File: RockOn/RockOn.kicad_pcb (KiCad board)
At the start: 2 copper layers, 10 parts

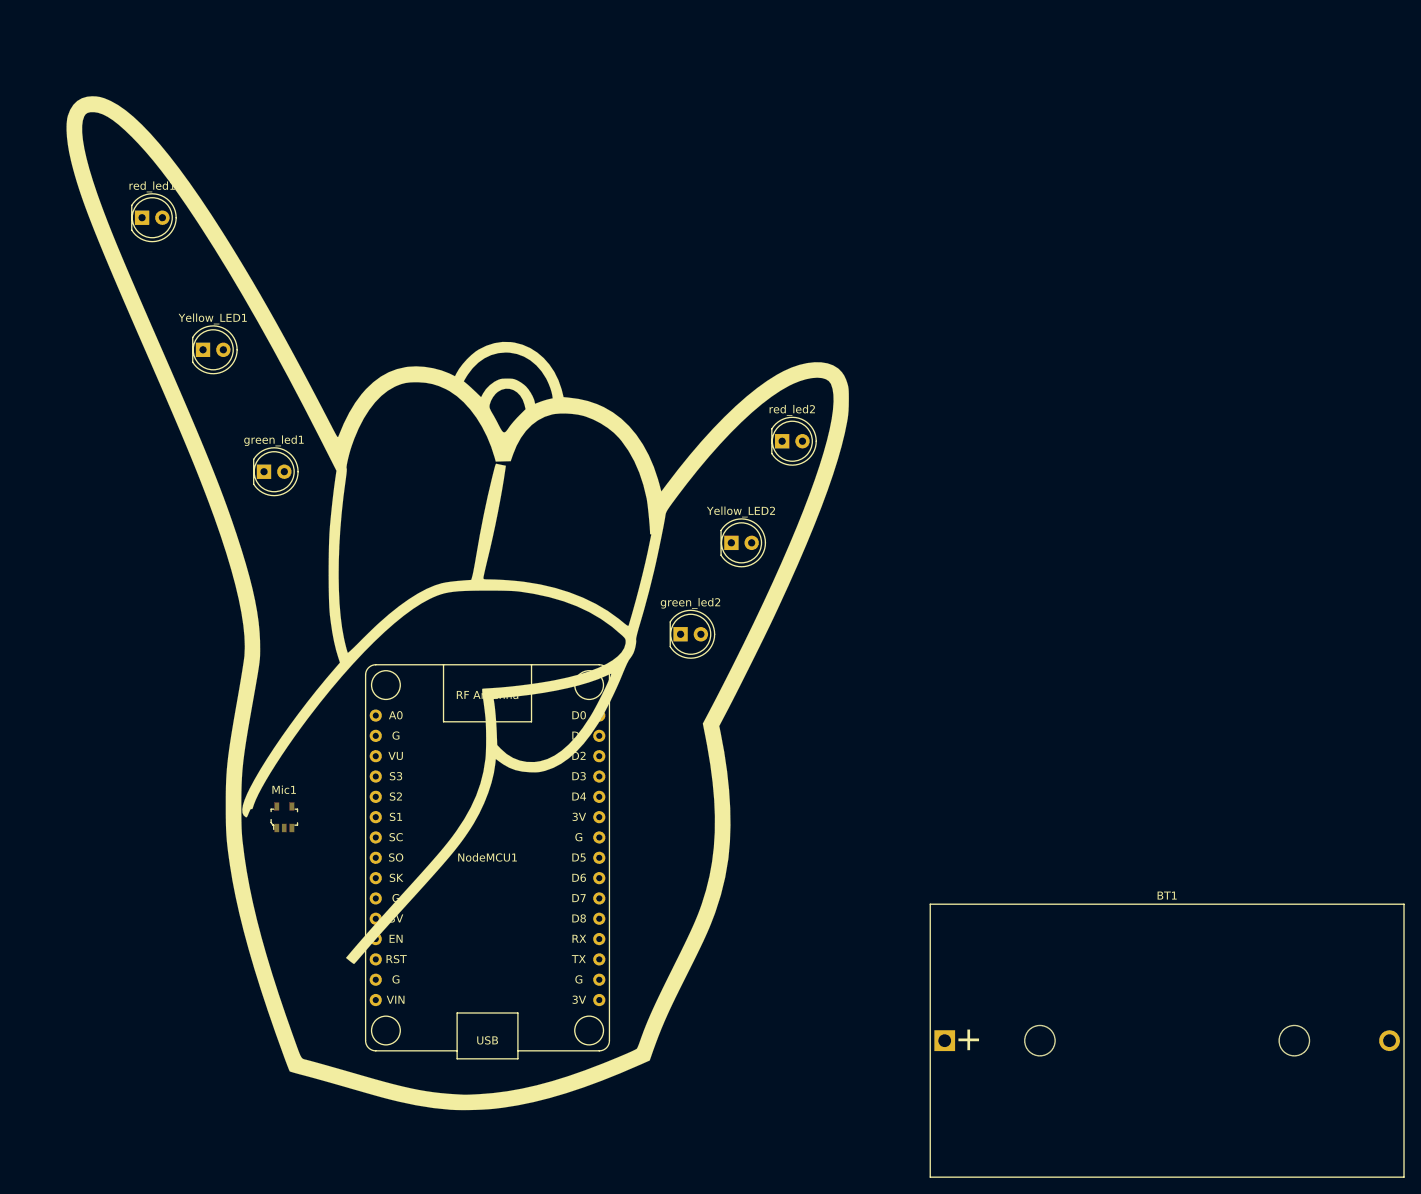
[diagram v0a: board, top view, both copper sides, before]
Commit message: Corrected components, silkscreen
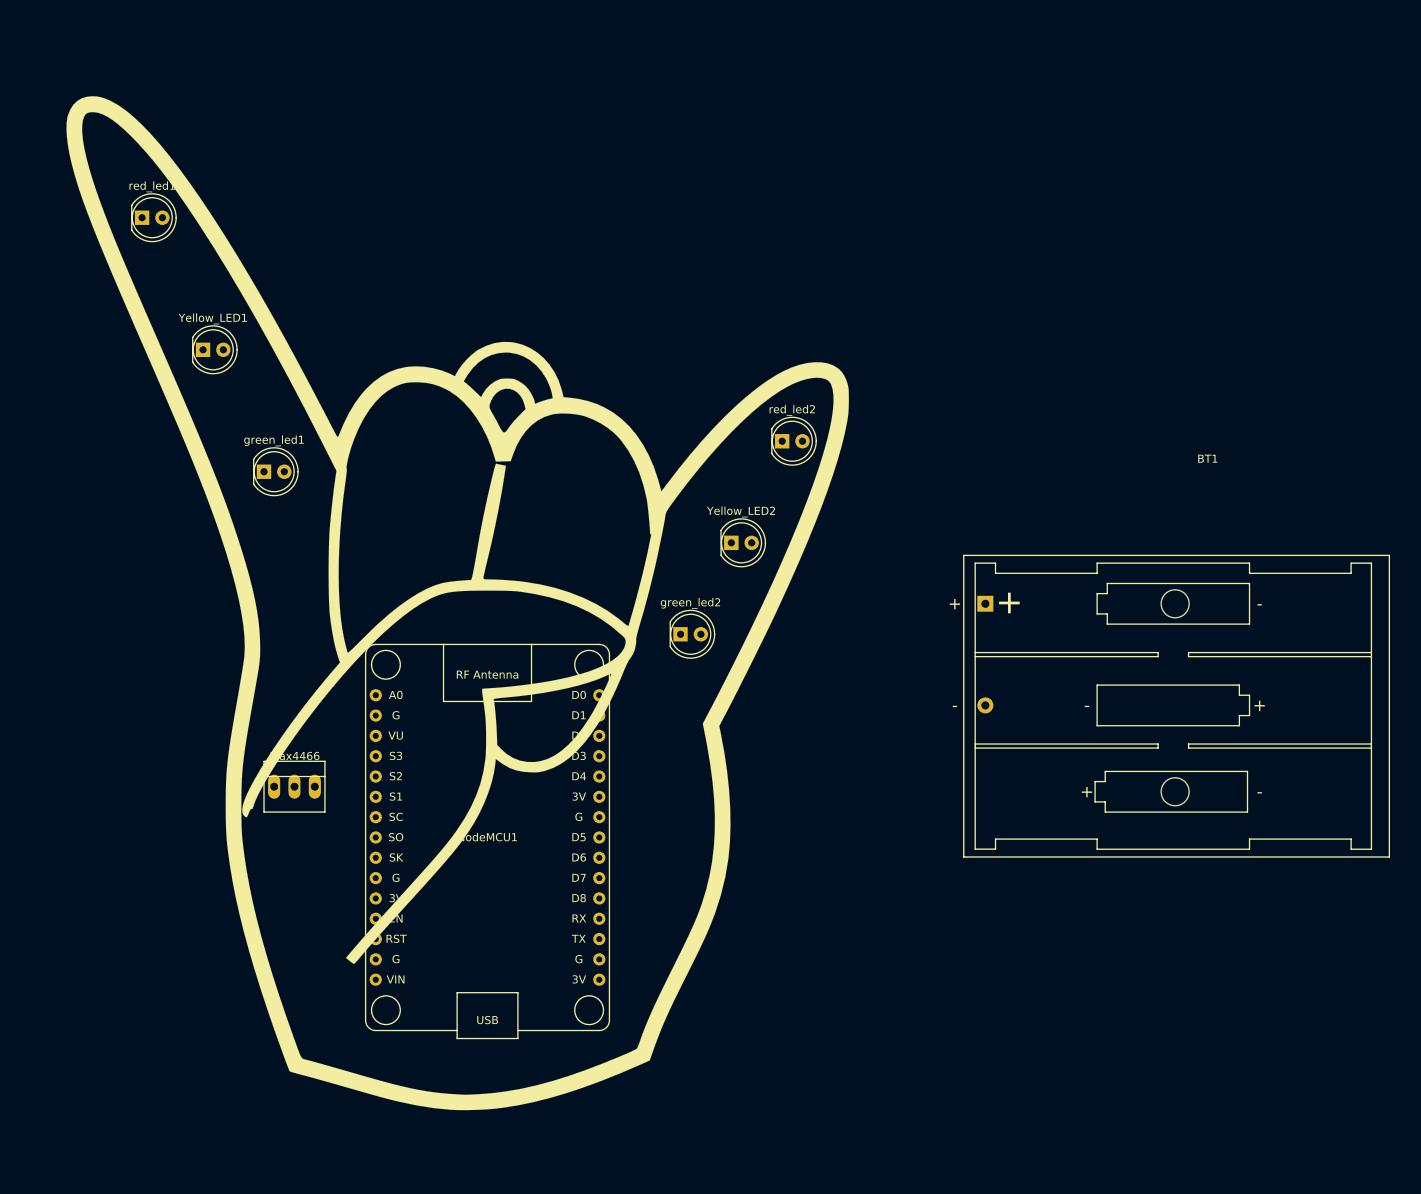
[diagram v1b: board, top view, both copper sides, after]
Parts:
- removed Mic1: MAX4466EXK_T, digikey-footprints:SOT-353
- added Max4466: Conn_01x03_Male, Connectors:PINHEAD1-3, F.Cu at (123.2, 133.3)
- BT1: footprint Battery_Holders:Bulgin_BX0036_1xC -> Battery_Holders:Keystone_2479_3xAAA
- moved BT1 54.8 mm to (212.1, 110.5)
- moved NodeMCU1 2.54 mm to (149.9, 139.7)

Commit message: larger silkscreen
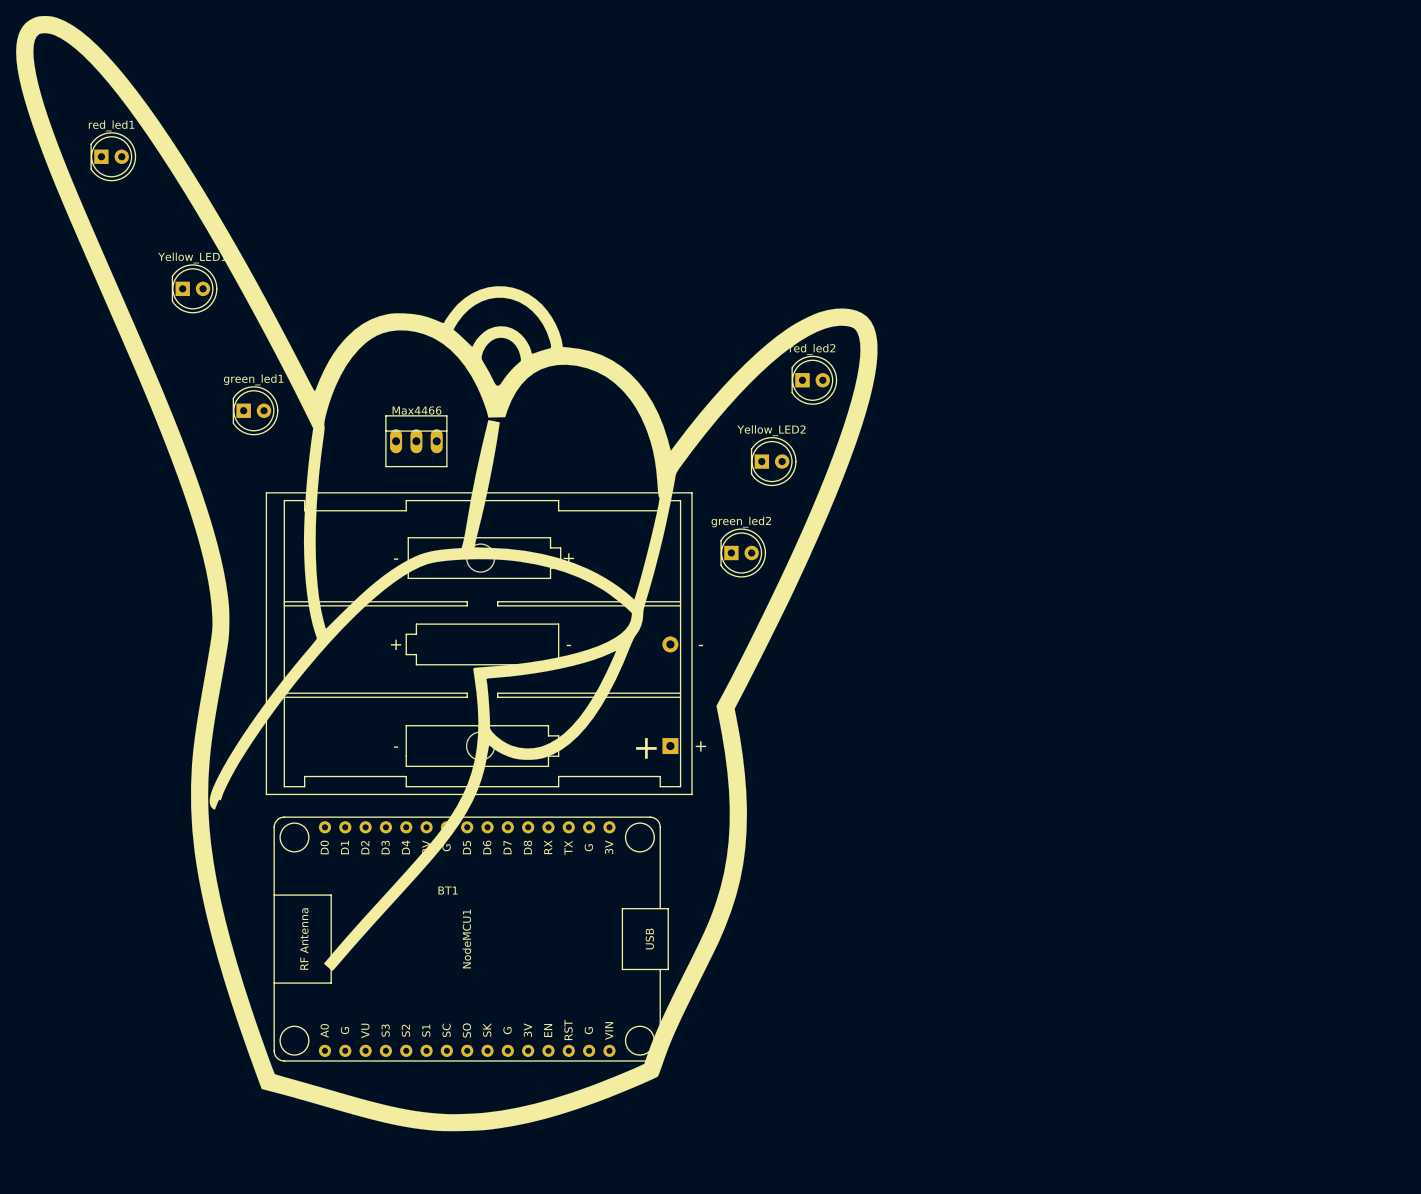
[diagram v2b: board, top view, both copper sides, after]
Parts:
- removed the G*** at (146.1, 108.0)
- added G***: LOGO, rockon:RockOn-silkscreen-110mm, F.Cu at (144.8, 106.7)
- moved Max4466 45.8 mm to (138.4, 90.2)
- moved BT1 43.2 mm to (172.7, 128.3), turned to 180 degrees
- moved NodeMCU1 13.0 mm to (147.3, 152.4), turned to 90 degrees
- moved green_led2 12.0 mm to (180.3, 104.1)
- moved Yellow_LED2 10.9 mm to (184.2, 92.7)
- moved red_led1 9.16 mm to (101.6, 54.6)
- moved green_led1 8.03 mm to (119.4, 86.4)
- moved red_led2 8.03 mm to (189.2, 82.5)
- moved Yellow_LED1 8.03 mm to (111.8, 71.1)

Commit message: Partially routed
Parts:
- moved Yellow_LED1 1.27 mm to (110.5, 71.1)
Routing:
- net Net-(Max4466-Pad3): track 0.00 -> 213.7 mm
- net Net-(Max4466-Pad1): track 0.00 -> 192.4 mm
- net Net-(Max4466-Pad2): track 0.00 -> 166.9 mm
- net Net-(NodeMCU1-Pad25): track 0.00 -> 109.5 mm
- net Net-(NodeMCU1-Pad29): track 0.00 -> 102.8 mm
- net Net-(NodeMCU1-Pad28): track 0.00 -> 77.3 mm
- net Net-(NodeMCU1-Pad22): track 0.00 -> 74.6 mm
- net Net-(NodeMCU1-Pad16): track 0.00 -> 66.9 mm
- net Net-(NodeMCU1-Pad23): track 0.00 -> 63.6 mm
- net Net-(BT1-Pad2): track 0.00 -> 62.2 mm
- net Net-(NodeMCU1-Pad21): track 0.00 -> 58.9 mm
- net Net-(NodeMCU1-Pad20): track 0.00 -> 44.8 mm
- net Net-(BT1-Pad1): track 0.00 -> 41.3 mm

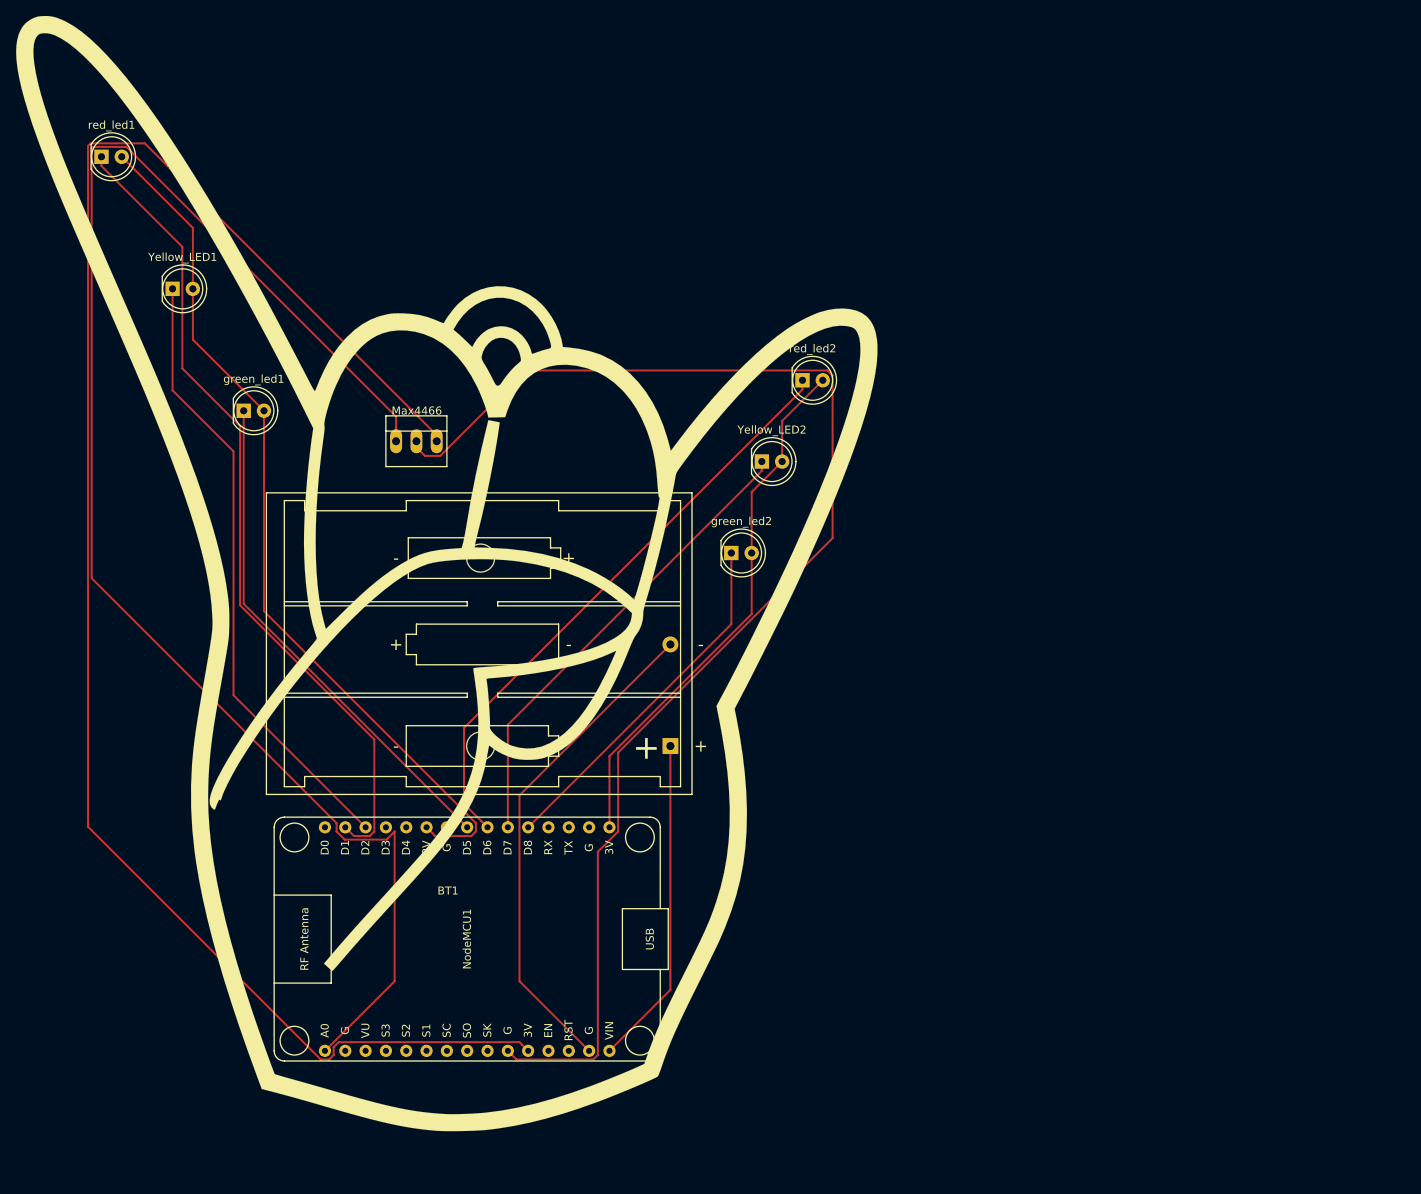
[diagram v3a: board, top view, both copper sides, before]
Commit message: Quick and lazy routing; needs refinement
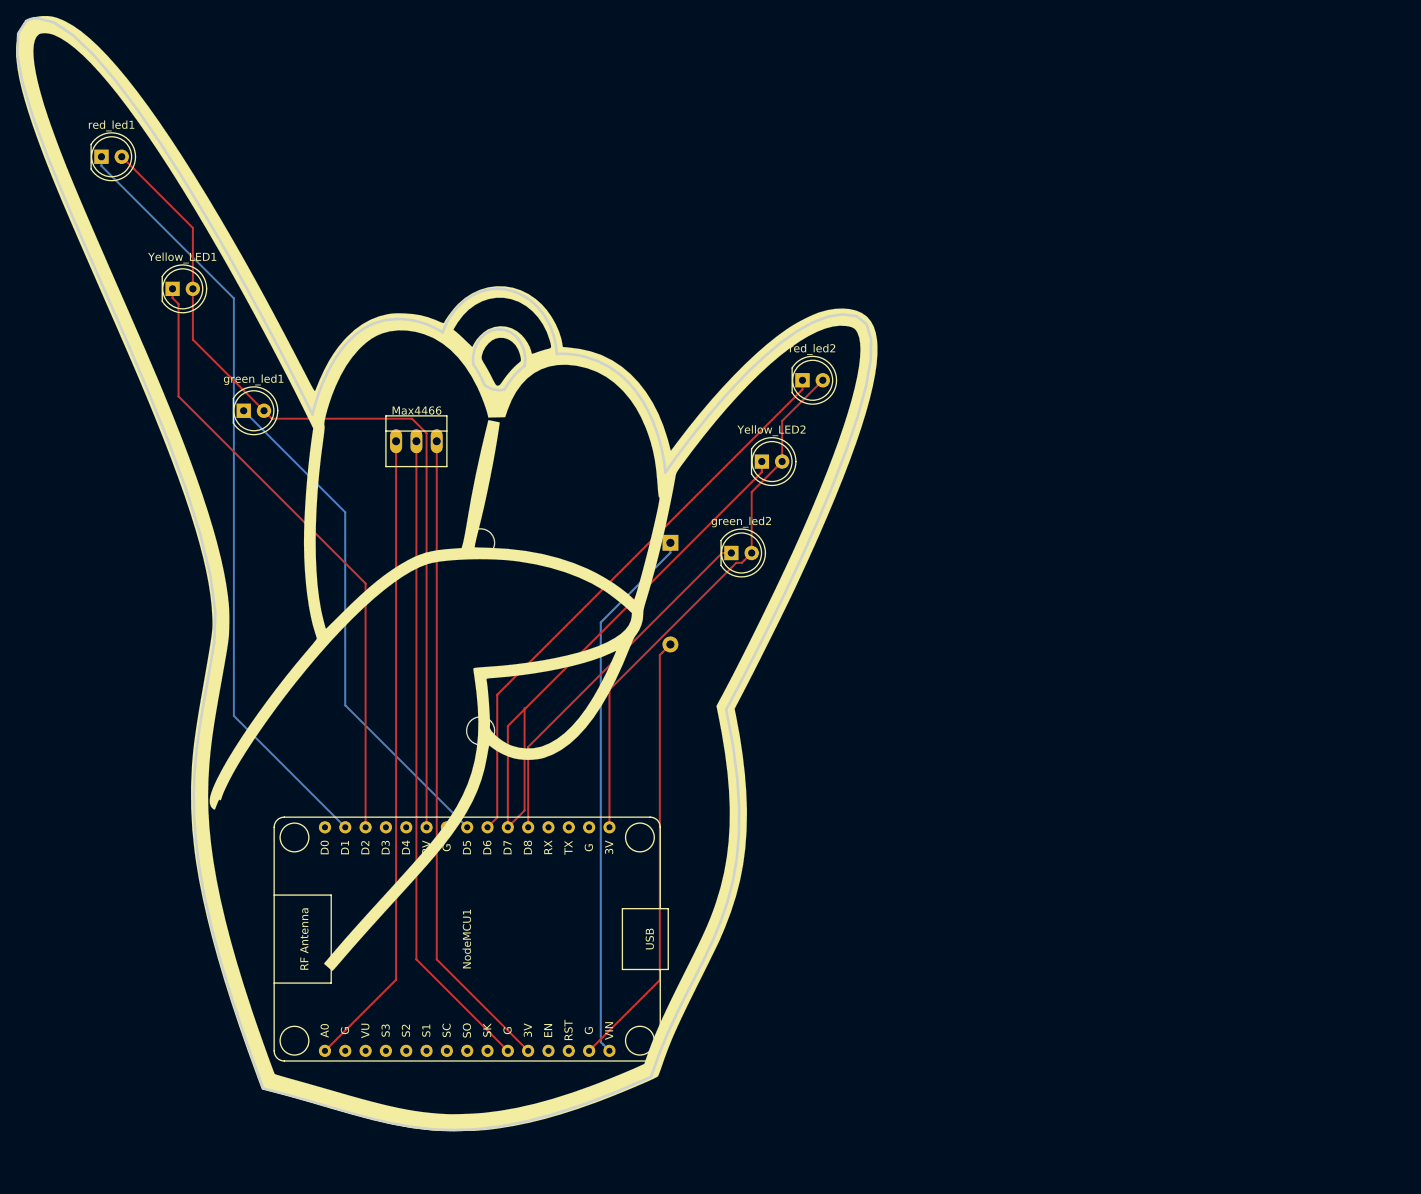
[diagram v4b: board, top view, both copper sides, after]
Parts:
- BT1: moved to B.Cu
- Edge1: renamed from G***; value LOGO -> Edge
- moved BT1 25.4 mm to (172.7, 102.9)
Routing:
- net Net-(Max4466-Pad3): track 213.7 -> 80.9 mm
- net Net-(Max4466-Pad1): track 192.4 -> 79.9 mm
- net Net-(Max4466-Pad2): track 166.9 -> 80.9 mm
- net Net-(BT1-Pad1): track 41.3 -> 67.6 mm
- net Net-(NodeMCU1-Pad21): track 58.9 -> 74.6 mm
- net Net-(BT1-Pad2): track 62.2 -> 55.0 mm
- net Net-(NodeMCU1-Pad29): track 102.8 -> 96.4 mm
- net Net-(NodeMCU1-Pad22): track 74.6 -> 72.2 mm
- net Net-(NodeMCU1-Pad20): track 44.8 -> 45.5 mm
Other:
- board outline added: 106.7 x 139 mm
